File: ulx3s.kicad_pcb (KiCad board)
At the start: 4 copper layers, 94 x 50.8 mm, 222 parts, among them J1 CONN_02X20, J2 CONN_02X20, J3 WIFI_OFF, J4 CONN_02X03, J5 VJ1, Q1 BC857, Q2 2N7002, SW1 SW_DIP_x04, U1 LFE5U-85F-6BG381C, U10 IS25LP128F-JBLE, U11 PCA9306D, U2 MT48LC16M16A2TG, U3 TLV62569DBV, U4 TLV62569DBV, U5 TLV62569DBV, U6 FT231XS, U7 MCP7940NT, U8 MAX11125, U9 ESP32, Y1 FNETHE025, Y2 32768Hz

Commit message: First pass cleanup
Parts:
- removed AE1: 433MHz, TestPoint:TestPoint_Pad_D1.0mm
- removed AUDIO1: JACK_TRS_6PINS, audio-jack:CUI_SJ-43516-SMT
- removed B0, B1, B2, B3, B4, B5, B6: PTS645, Button_Switch_SMD:SW_SPST_PTS645
- removed BAT1: CR1225, Keystone_3000_1x12mm-CoinCell:Keystone_3000_1x12mm-CoinCell
- removed C14, C59, C60, C62: 220nF, Capacitor_SMD:C_0603_1608Metric
- removed C15, C21, C54, C55, C58, C61: 22uF, Capacitor_SMD:C_0805_2012Metric
- removed C16, C47: 2.2uF, Capacitor_SMD:C_0805_2012Metric
- removed C18: 470pF, Capacitor_SMD:C_0603_1608Metric
- removed C33, C34, C35, C52: 22nF, Capacitor_SMD:C_0603_1608Metric
- removed C56, C57: 4.7pF, Capacitor_SMD:C_0603_1608Metric
- removed D0, D11, D4: RED, LED_SMD:LED_0805_2012Metric
- removed D1, D5: ORANGE, LED_SMD:LED_0805_2012Metric
- removed D10, D13, D14, D16, D17, D27: 1N914, Diode_SMD:D_SOD-323_HandSoldering
- removed D12, D15: BAT54W, Diode_SMD:D_SOD-323_HandSoldering
- removed D2, D6: GREEN, LED_SMD:LED_0805_2012Metric
- removed D3, D7: BLUE, LED_SMD:LED_0805_2012Metric
- removed D51, D52: 0, jumper:D_SMA_Jumper_NC
- removed HR: HR, hrvatski_proizvod_veci:hrvatski
- removed J1, J2: CONN_02X20, Socket_Strips:Socket_Strip_Angled_2x20
- removed J3: WIFI_OFF, Connector_PinHeader_2.54mm:PinHeader_1x02_P2.54mm_Vertical
- removed J5: VJ1, Connector_PinHeader_2.54mm:PinHeader_1x03_P2.54mm_Vertical
- removed L4, L5: 33uH, Inductor_SMD:L_0805_2012Metric_Pad1.15x1.40mm_HandSolder
- removed LCD1: ST7789, st7789:st7789
- removed Q1: BC857, Package_TO_SOT_SMD:SOT-23
- removed Q2: 2N7002, Package_TO_SOT_SMD:SOT-23
- removed R1, R25, R26, R3, R4: 4.7k, Resistor_SMD:R_0603_1608Metric
- removed R10, R17, R21, R39, R51, R60, R7: 130, Resistor_SMD:R_0603_1608Metric
- removed R13, R34, R9: 15k, Resistor_SMD:R_0603_1608Metric
- removed R14, R18, R57, R6, R66, R8: 1.1k, Resistor_SMD:R_0603_1608Metric
- removed R15, R19, R35, R41, R42, R43, R44, R45, R46, R47, R48, R58, R65: 549, Resistor_SMD:R_0603_1608Metric
- removed R16, R20, R59: 270, Resistor_SMD:R_0603_1608Metric
- removed R2: 18k, Resistor_SMD:R_0603_1608Metric
- removed R22, R23: 3.3k, Resistor_SMD:R_0603_1608Metric
- removed R24: 100k, Resistor_SMD:R_0603_1608Metric
- removed R38: 0.47, Resistor_SMD:R_0603_1608Metric
- removed R5: 2.2M, Resistor_SMD:R_0603_1608Metric
- removed R56: 0, Resistor_SMD:R_0603_1608Metric
- removed REF** (x2): emard12mm, emard:emard12mm
- removed REF**: inem, inem:inem
- removed RV2, RV3: 0, Resistor_SMD:R_0805_2012Metric_Pad1.29x1.40mm_HandSolder
- removed SD1: 104031-0811, micro-sd-104031-811:MOLEX_104031-0811
- removed SW1: SW_DIP_x04, dipswitch:SW_DIP_x4_W8.61mm_Slide_LowProfile
- removed U11: PCA9306D, SM8:SM8
- removed U2: MT48LC16M16A2TG, TSOP54:TSOP54
- removed U6: FT231XS, ft231x:FT231X-SSOP-20_4.4x6.5mm_Pitch0.65mm
- removed U7: MCP7940NT, SOT96-1:SOT96-1
- removed U8: MAX11125, max1112x-tqfn28:MAX1112x-TQFN-28-1EP_5x5mm_Pitch0.5mm
- removed U9: ESP32, ESP32:ESP32
- removed Y2: 32768Hz, abs25:Crystal_SMD_ABS25
- removed fer: fer, fer:fer
- removed koncar: koncar, koncar:koncar
- removed radiona: radiona, radiona:radiona
- C13: moved to F.Cu
- moved C13 46.9 mm to (133.6, 59.5), turned to 0 degrees
- moved C51 17.8 mm to (162.7, 98.2)
- moved C50 11.6 mm to (169.2, 81.9)
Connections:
- C13 pad 1: +5V -> GND
- C13 pad 2: /power/WKUP -> 2V5_3V3
- C20 pad 1: +3V3 -> 2V5_3V3
- C25 pad 1: +3V3 -> 2V5_3V3
- C31 pad 1: +3V3 -> 2V5_3V3
- C32 pad 1: +3V3 -> 2V5_3V3
- C46 pad 1: +3V3 -> 2V5_3V3
- C50 pad 1: +3V3 -> 2V5_3V3
- C51 pad 1: +3V3 -> 2V5_3V3
- D18 pad 2: FTDI_nSLEEP -> (no net)
- D19 pad 2: FT2V5 -> (no net)
- D28 pad 1: PWRBTn -> (no net)
- GPDI1 pad 15: GPDI_SCL -> (no net)
- GPDI1 pad 16: GPDI_SDA -> (no net)
- J4 pad 2: +3V3 -> 2V5_3V3
- R11 pad 1: +3V3 -> 2V5_3V3
- R12 pad 1: +3V3 -> 2V5_3V3
- R27 pad 1: +3V3 -> 2V5_3V3
- R28 pad 1: +3V3 -> 2V5_3V3
- R29 pad 1: +3V3 -> 2V5_3V3
- R30 pad 1: +3V3 -> 2V5_3V3
- R31 pad 1: +3V3 -> 2V5_3V3
- R32 pad 1: +3V3 -> 2V5_3V3
- R33 pad 1: +3V3 -> 2V5_3V3
- R37 pad 1: FTDI_nTXLED -> (no net)
- R49 pad 1: USB_FTDI_D- -> (no net)
- R50 pad 1: USB_FTDI_D+ -> (no net)
- R62 pad 2: +3V3 -> 2V5_3V3
- RP3 pad 2: +3V3 -> 2V5_3V3
- U1 pad A10: GP1 -> (no net)
- U1 pad A11: GN1 -> (no net)
- U1 pad A15: Net-(U1-PadA15) -> (no net)
- U1 pad A2: GP9 -> (no net)
- U1 pad A3: AUDIO_R0 -> (no net)
- U1 pad A4: GP8 -> (no net)
- U1 pad A5: GN8 -> (no net)
- U1 pad A6: GP7 -> (no net)
- U1 pad A7: GP4 -> (no net)
- U1 pad A8: GN4 -> (no net)
- U1 pad A9: GP2 -> (no net)
- U1 pad B1: GN9 -> (no net)
- U1 pad B10: GN2 -> (no net)
- U1 pad B11: GP0 -> (no net)
- U1 pad B13: GP26 -> (no net)
- U1 pad B15: GP22 -> (no net)
- U1 pad B17: GP23 -> (no net)
- U1 pad B19: FPDI_SDA -> (no net)
- U1 pad B2: LED0 -> (no net)
- U1 pad B3: AUDIO_L3 -> (no net)
- U1 pad B4: GN10 -> (no net)
- U1 pad B5: AUDIO_R1 -> (no net)
- U1 pad B6: GN7 -> (no net)
- U1 pad B8: GN5 -> (no net)
- U1 pad B9: GP3 -> (no net)
- U1 pad C1: LED2 -> (no net)
- U1 pad C10: GN3 -> (no net)
- U1 pad C11: GN0 -> (no net)
- U1 pad C13: GN26 -> (no net)
- U1 pad C15: GN22 -> (no net)
- U1 pad C16: GP24 -> (no net)
- U1 pad C17: GN23 -> (no net)
- U1 pad C18: GP21 -> (no net)
- U1 pad C2: LED1 -> (no net)
- U1 pad C20: SDRAM_D11 -> (no net)
- U1 pad C3: AUDIO_L2 -> (no net)
- U1 pad C4: GP10 -> (no net)
- U1 pad C5: AUDIO_R3 -> (no net)
- U1 pad C6: GP6 -> (no net)
- U1 pad C7: GN6 -> (no net)
- U1 pad C8: GP5 -> (no net)
- U1 pad C9: Net-(U1-PadC9) -> (no net)
- U1 pad D1: LED4 -> (no net)
- U1 pad D10: Net-(U1-PadD10) -> (no net)
- U1 pad D11: Net-(U1-PadD11) -> (no net)
- U1 pad D12: Net-(U1-PadD12) -> (no net)
- U1 pad D13: GP27 -> (no net)
- U1 pad D14: GP25 -> (no net)
- U1 pad D16: GN24 -> (no net)
- U1 pad D17: GN21 -> (no net)
- U1 pad D18: GP20 -> (no net)
- U1 pad D19: SDRAM_D10 -> (no net)
- U1 pad D2: LED3 -> (no net)
- U1 pad D20: SDRAM_D9 -> (no net)
- U1 pad D3: AUDIO_L1 -> (no net)
- U1 pad D5: AUDIO_R2 -> (no net)
- U1 pad D6: BTN_PWRn -> (no net)
- U1 pad D7: SW3 -> (no net)
- U1 pad D8: SW2 -> (no net)
- U1 pad D9: Net-(U1-PadD9) -> (no net)
- U1 pad E1: LED6 -> (no net)
- U1 pad E10: Net-(U1-PadE10) -> (no net)
- U1 pad E11: Net-(U1-PadE11) -> (no net)
- U1 pad E12: FPDI_SCL -> (no net)
- U1 pad E13: GN27 -> (no net)
- U1 pad E14: GN25 -> (no net)
- U1 pad E17: GN20 -> (no net)
- U1 pad E18: SDRAM_D12 -> (no net)
- U1 pad E19: SDRAM_D8 -> (no net)
- U1 pad E2: LED5 -> (no net)
- U1 pad E20: SDRAM_DQM1 -> (no net)
- U1 pad E3: GN11 -> (no net)
- U1 pad E4: AUDIO_L0 -> (no net)
- U1 pad E5: AUDIO_V3 -> (no net)
- U1 pad E6: WIFI_GPIO35 -> (no net)
- U1 pad E7: SW4 -> (no net)
- U1 pad E8: SW1 -> (no net)
- U1 pad E9: WIFI_GPIO25 -> (no net)
- U1 pad F1: WIFI_EN -> (no net)
- U1 pad F11: +3V3 -> 2V5_3V3
- U1 pad F12: +3V3 -> 2V5_3V3
- U1 pad F17: GP19 -> (no net)
- U1 pad F18: SDRAM_D13 -> (no net)
- U1 pad F19: SDRAM_CLK -> (no net)
- U1 pad F2: AUDIO_V1 -> (no net)
- U1 pad F20: SDRAM_CKE -> (no net)
- U1 pad F3: GN12 -> (no net)
- U1 pad F4: GP11 -> (no net)
- U1 pad F5: AUDIO_V2 -> (no net)
- U1 pad G16: SHUTDOWN -> (no net)
- U1 pad G18: GN19 -> (no net)
- U1 pad G19: SDRAM_A12 -> (no net)
- U1 pad G20: SDRAM_A11 -> (no net)
- U1 pad G3: GP12 -> (no net)
- U1 pad G5: GN13 -> (no net)
- U1 pad H1: SD_D1 -> (no net)
- U1 pad H14: +3V3 -> 2V5_3V3
- U1 pad H15: +3V3 -> 2V5_3V3
- U1 pad H16: BTN_R -> (no net)
- U1 pad H17: GN18 -> (no net)
- U1 pad H18: GP18 -> (no net)
- U1 pad H2: SD_CLK -> (no net)
- U1 pad H20: SDRAM_A9 -> (no net)
- U1 pad H3: LED7 -> (no net)
- U1 pad H4: GP13 -> (no net)
- U1 pad H5: AUDIO_V0 -> (no net)
- U1 pad J1: SD_CMD -> (no net)
- U1 pad J15: +3V3 -> 2V5_3V3
- U1 pad J16: SDRAM_D0 -> (no net)
- U1 pad J17: SDRAM_D15 -> (no net)
- U1 pad J18: SDRAM_D14 -> (no net)
- U1 pad J19: SDRAM_A8 -> (no net)
- U1 pad J20: SDRAM_A7 -> (no net)
- U1 pad J3: SD_D0 -> (no net)
- U1 pad J4: OLED_BL -> (no net)
- U1 pad J5: WIFI_GPIO22 -> (no net)
- U1 pad K1: SD_D2 -> (no net)
- U1 pad K16: Net-(U1-PadK16) -> (no net)
- U1 pad K17: Net-(U1-PadK17) -> (no net)
- U1 pad K18: SDRAM_A6 -> (no net)
- U1 pad K19: SDRAM_A5 -> (no net)
- U1 pad K2: SD_D3 -> (no net)
- U1 pad K20: SDRAM_A4 -> (no net)
- U1 pad K3: WIFI_RXD -> (no net)
- U1 pad K4: WIFI_TXD -> (no net)
- U1 pad K5: WIFI_GPIO21 -> (no net)
- U1 pad L1: WIFI_GPIO26 -> (no net)
- U1 pad L14: +3V3 -> 2V5_3V3
- U1 pad L15: +3V3 -> 2V5_3V3
- U1 pad L16: GP17 -> (no net)
- U1 pad L17: GN17 -> (no net)
- U1 pad L18: SDRAM_D1 -> (no net)
- U1 pad L19: SDRAM_A3 -> (no net)
- U1 pad L2: WIFI_GPIO0 -> (no net)
- U1 pad L20: SDRAM_A2 -> (no net)
- U1 pad L3: FTDI_TXDEN -> (no net)
- U1 pad L4: FTDI_RXD -> (no net)
- U1 pad L5: FTDI_nRXLED -> (no net)
- U1 pad L6: +3V3 -> 2V5_3V3
- U1 pad L7: +3V3 -> 2V5_3V3
- U1 pad M1: FTDI_TXD -> (no net)
- U1 pad M15: +3V3 -> 2V5_3V3
- U1 pad M17: GN16 -> (no net)
- U1 pad M18: SDRAM_D2 -> (no net)
- U1 pad M19: SDRAM_A1 -> (no net)
- U1 pad M20: SDRAM_A0 -> (no net)
- U1 pad M3: FTDI_nRTS -> (no net)
- U1 pad M5: Net-(U1-PadM5) -> (no net)
- U1 pad M6: +3V3 -> 2V5_3V3
- U1 pad N1: FTDI_nDTR -> (no net)
- U1 pad N16: GP16 -> (no net)
- U1 pad N17: GP15 -> (no net)
- U1 pad N18: SDRAM_D3 -> (no net)
- U1 pad N19: SDRAM_A10 -> (no net)
- U1 pad N2: OLED_CS -> (no net)
- U1 pad N20: SDRAM_BA1 -> (no net)
- U1 pad N3: WIFI_GPIO27 -> (no net)
- U1 pad N4: WIFI_GPIO19 -> (no net)
- U1 pad N5: SD_CD -> (no net)
- U1 pad P1: OLED_DC -> (no net)
- U1 pad P10: +3V3 -> 2V5_3V3
- U1 pad P16: GN15 -> (no net)
- U1 pad P17: ADC_SCLK -> (no net)
- U1 pad P18: SDRAM_D4 -> (no net)
- U1 pad P19: SDRAM_BA0 -> (no net)
- U1 pad P2: OLED_RES -> (no net)
- U1 pad P20: SDRAM_nCS -> (no net)
- U1 pad P3: OLED_MOSI -> (no net)
- U1 pad P4: OLED_CLK -> (no net)
- U1 pad P5: SD_WP -> (no net)
- U1 pad P9: +3V3 -> 2V5_3V3
- U1 pad R1: BTN_F1 -> (no net)
- U1 pad R16: ADC_MOSI -> (no net)
- U1 pad R17: ADC_CSn -> (no net)
- U1 pad R18: BTN_U -> (no net)
- U1 pad R20: SDRAM_nRAS -> (no net)
- U1 pad R3: Net-(U1-PadR3) -> (no net)
- U1 pad T1: BTN_F2 -> (no net)
- U1 pad T16: Net-(U1-PadT16) -> (no net)
- U1 pad T17: SDRAM_D6 -> (no net)
- U1 pad T18: SDRAM_D5 -> (no net)
- U1 pad T19: SDRAM_nCAS -> (no net)
- U1 pad T2: +3V3 -> 2V5_3V3
- U1 pad T20: SDRAM_nWE -> (no net)
- U1 pad T3: +3V3 -> 2V5_3V3
- U1 pad T4: +3V3 -> 2V5_3V3
- U1 pad U1: BTN_L -> (no net)
- U1 pad U16: ADC_MISO -> (no net)
- U1 pad U17: GN14 -> (no net)
- U1 pad U18: GP14 -> (no net)
- U1 pad U19: SDRAM_DQM0 -> (no net)
- U1 pad U2: +3V3 -> 2V5_3V3
- U1 pad U20: SDRAM_D7 -> (no net)
- U1 pad V1: BTN_D -> (no net)
- U1 pad W13: Net-(U1-PadW13) -> (no net)
- U1 pad W14: Net-(U1-PadW14) -> (no net)
- U1 pad W17: Net-(U1-PadW17) -> (no net)
- U1 pad W18: Net-(U1-PadW18) -> (no net)
- U1 pad W20: Net-(U1-PadW20) -> (no net)
- U1 pad W4: Net-(U1-PadW4) -> (no net)
- U1 pad W5: Net-(U1-PadW5) -> (no net)
- U1 pad W8: Net-(U1-PadW8) -> (no net)
- U1 pad W9: Net-(U1-PadW9) -> (no net)
- U1 pad Y11: Net-(U1-PadY11) -> (no net)
- U1 pad Y12: Net-(U1-PadY12) -> (no net)
- U1 pad Y14: Net-(U1-PadY14) -> (no net)
- U1 pad Y15: Net-(U1-PadY15) -> (no net)
- U1 pad Y16: Net-(U1-PadY16) -> (no net)
- U1 pad Y17: Net-(U1-PadY17) -> (no net)
- U1 pad Y19: Net-(U1-PadY19) -> (no net)
- U1 pad Y5: Net-(U1-PadY5) -> (no net)
- U1 pad Y6: Net-(U1-PadY6) -> (no net)
- U1 pad Y7: Net-(U1-PadY7) -> (no net)
- U1 pad Y8: Net-(U1-PadY8) -> (no net)
- U10 pad 8: +3V3 -> 2V5_3V3
- U3 pad 1: /power/PWREN -> +5V
- U4 pad 1: /power/PWREN -> +5V
- U5 pad 1: /power/PWREN -> +5V
- US1 pad 4: Net-(US1-Pad4) -> (no net)
- US2 pad 4: US2_ID -> (no net)
- Y1 pad 1: +3V3 -> 2V5_3V3
- Y1 pad 4: +3V3 -> 2V5_3V3
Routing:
- net (no net): track 0.00 -> 834.9 mm, vias 0 -> 160
- net +3V3: track 184.1 -> 0.00 mm, vias 33 -> 0
- net GND: track 458.6 -> 304.4 mm, vias 136 -> 124
- net /power/PWREN: track 115.6 -> 0.00 mm, vias 3 -> 0
- net /usb/ANT_433MHz: track 111.7 -> 4.23 mm, vias 2 -> 0
- net FPDI_SDA: track 91.9 -> 0.00 mm, vias 6 -> 0
- net FPDI_SCL: track 89.0 -> 0.00 mm, vias 4 -> 0
- net +5V: track 149.0 -> 233.3 mm, vias 7 -> 9
- net /blinkey/BTNPUR: track 76.6 -> 0.00 mm, vias 3 -> 0
- net BTN_R: track 70.5 -> 0.00 mm, vias 4 -> 0
- net GP15: track 58.6 -> 0.00 mm, vias 2 -> 0
- net USB_FTDI_D+: track 58.5 -> 0.00 mm, vias 2 -> 0
- net GP14: track 58.1 -> 0.00 mm, vias 1 -> 0
- net GP17: track 58.0 -> 0.00 mm, vias 2 -> 0
- net GP16: track 57.0 -> 0.00 mm, vias 1 -> 0
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- removed copper zone on In1.Cu, net +3V3
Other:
- board text removed: "+-"
- board text removed: "-+"
- board text removed: "0"
- board text removed: "1"
- board text removed: "10"
- board text removed: "11"
- board text removed: "12"
- board text removed: "13"
- board text removed: "14"
- board text removed: "15"
- board text removed: "16"
- board text removed: "17"
- board text removed: "18"
- board text removed: "19"
- board text removed: "2"
- board text removed: "2.5/3.3V"
- board text removed: "2.5V"
- board text removed: "20"
- board text removed: "21"
- board text removed: "22"
- board text removed: "23"
- board text removed: "24"
- board text removed: "25"
- board text removed: "26"
- board text removed: "27"
- board text removed: "3"
- board text removed: "3.3V"
- board text removed: "3V 12.5x2.5mm"
- board text removed: "4"
- board text removed: "5"
- board text removed: "5V"
- board text removed: "6"
- board text removed: "7"
- board text removed: "8"
- board text removed: "9"
- board text removed: "ADC"
- board text removed: "CR1225"
- board text removed: "DOWN"
- board text removed: "F1"
- board text removed: "F2"
- board text removed: "LEFT"
- board text removed: "PWR"
- board text removed: "RIGHT"
- board text removed: "RTC"
- board text removed: "SDRAM"
- board text removed: "UP"
- board text removed: "skriptarnica.hr"

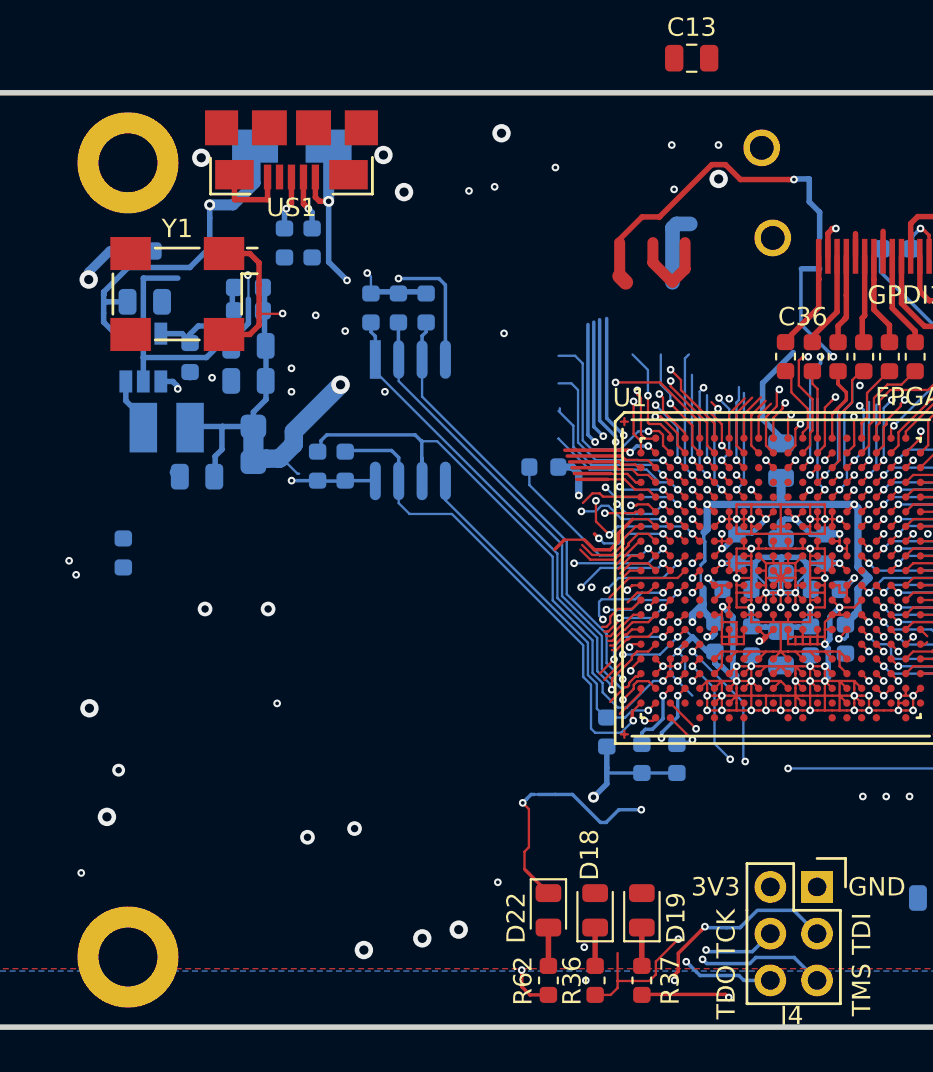
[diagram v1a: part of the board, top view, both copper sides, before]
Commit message: More cleanup - moving flash and crystal
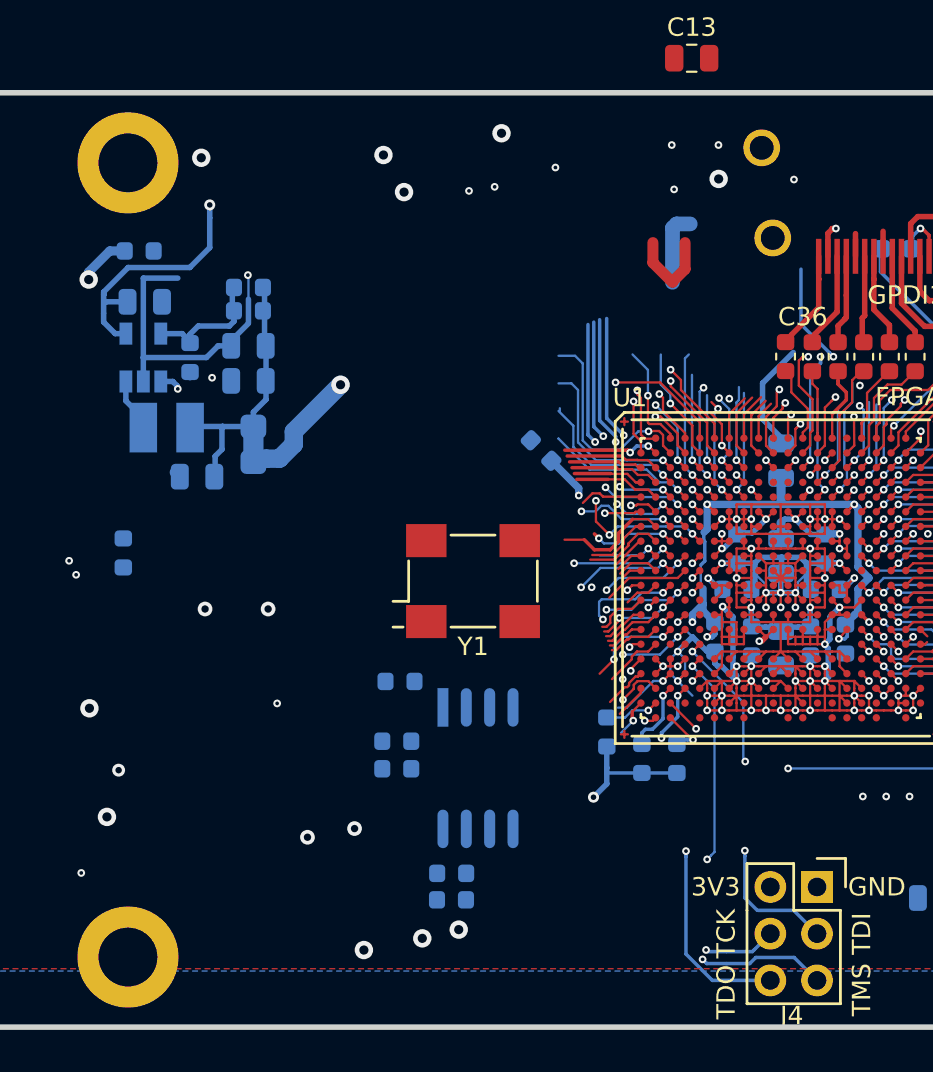
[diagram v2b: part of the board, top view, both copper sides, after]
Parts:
- removed D18: GREEN, LED_SMD:LED_0805_2012Metric
- removed D19: RED, LED_SMD:LED_0805_2012Metric
- removed D22: BLUE, LED_SMD:LED_0805_2012Metric
- removed D8: STPS2L40AF, Diode_SMD:D_SMA
- removed R36, R37, R62: 549, Resistor_SMD:R_0603_1608Metric
- removed R49, R50: 27, Resistor_SMD:R_0603_1608Metric
- removed US1: MICRO_USB, usb_otg:USB-MICRO-B-FCI-10118192-0001LF
- moved R11 25.1 mm to (117.6, 98.2), turned to 0 degrees
- moved R29 24.7 mm to (120.6, 105.3), turned to 0 degrees
- moved R28 23.6 mm to (117.6, 96.7), turned to 0 degrees
- moved R12 22.9 mm to (120.6, 103.9), turned to 0 degrees
- moved Y1 22.4 mm to (121.8, 88.0), turned to 0 degrees
- moved R30 20.4 mm to (117.8, 93.4), turned to 0 degrees
- moved U10 19.3 mm to (122.0, 98.1)
- moved C53 0.91 mm to (125.5, 80.9), turned to 135 degrees
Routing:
- net USB5V: track 52.1 -> 0.00 mm, vias 3 -> 0
- net /flash/FLASH_SCK: track 32.7 -> 3.62 mm
- net /flash/FLASH_nCS: track 29.6 -> 3.25 mm, vias 1 -> 0
- net GND: track 304.4 -> 278.2 mm, vias 124 -> 117
- net /flash/FLASH_MISO: track 28.3 -> 2.49 mm
- net /flash/FLASH_nHOLD: track 27.3 -> 2.11 mm
- net /flash/FLASH_nWP: track 27.4 -> 3.43 mm
- net +2V5: track 123.8 -> 103.7 mm
- net 2V5_3V3: track 174.1 -> 154.0 mm, vias 30 -> 25
- net /flash/FLASH_MOSI: track 19.5 -> 2.98 mm
- net JTAG_TMS: track 39.4 -> 23.2 mm, vias 4 -> 2
- net (no net): track 834.9 -> 820.1 mm, vias 160 -> 159
- net JTAG_TDO: track 35.1 -> 20.7 mm, vias 4 -> 3
- net JTAG_TDI: track 33.7 -> 19.9 mm, vias 5 -> 3
- net +5V: track 233.3 -> 228.4 mm
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
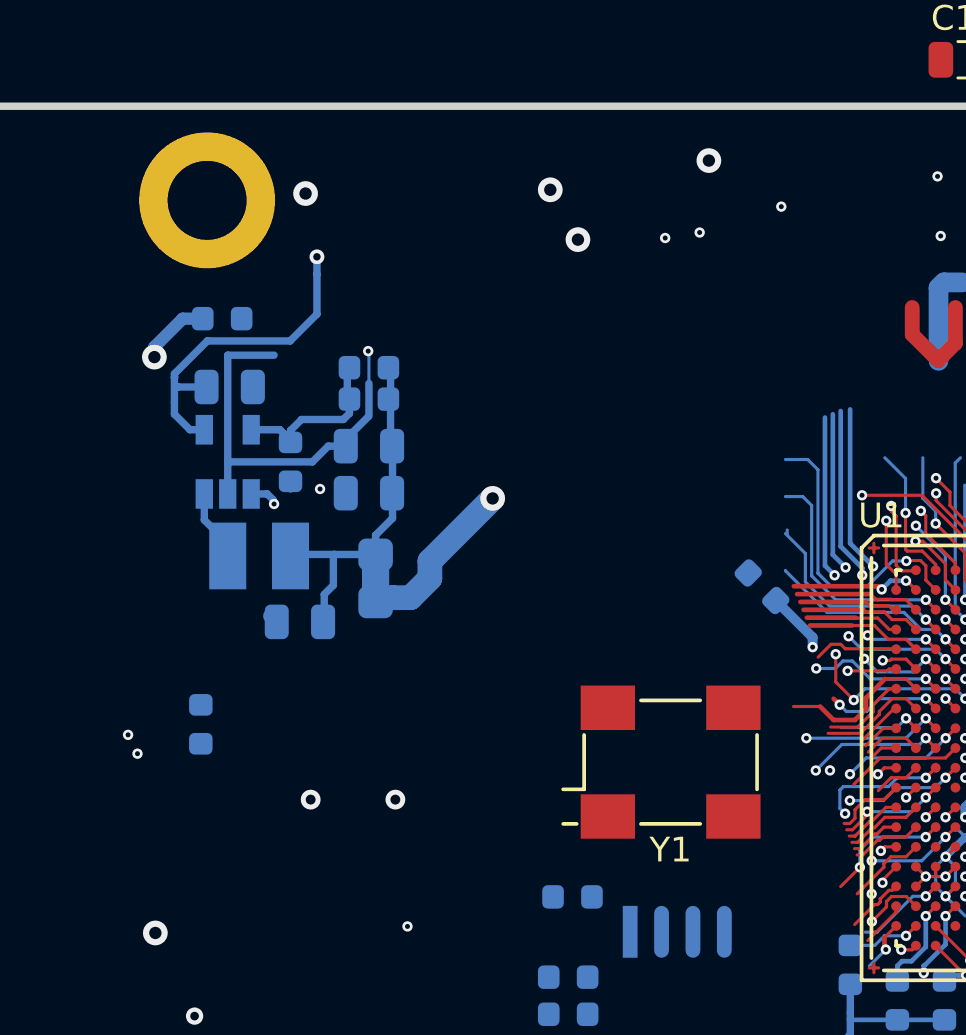
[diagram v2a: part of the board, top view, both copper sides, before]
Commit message: Moving power closer
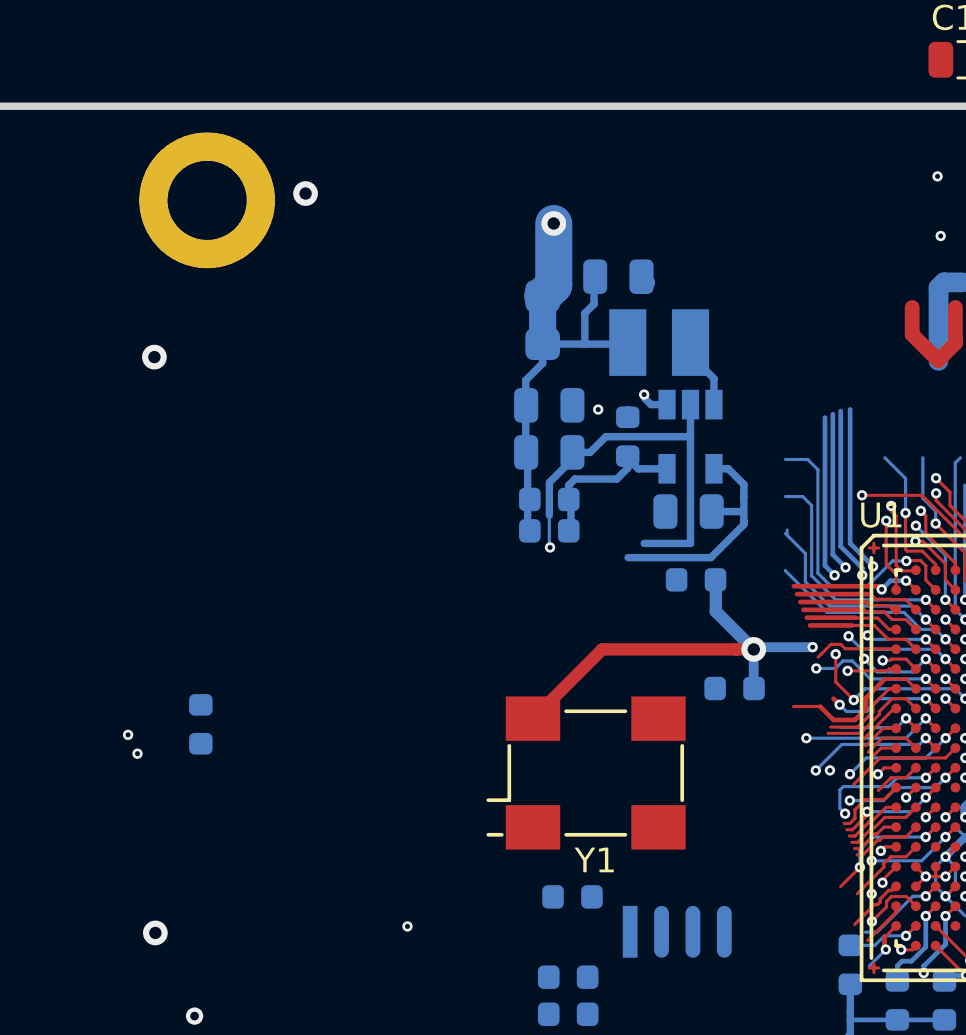
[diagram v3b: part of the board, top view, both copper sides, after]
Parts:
- moved C48 21.9 mm to (122.8, 80.6), turned to 180 degrees
- moved C1 19.2 mm to (122.5, 77.8), turned to 180 degrees
- moved C23 19.0 mm to (119.6, 68.3), turned to 0 degrees
- moved U4 18.8 mm to (122.6, 74.8), turned to 0 degrees
- moved L2 18.4 mm to (121.3, 71.0), turned to 180 degrees
- moved RB2 13.7 mm to (120.0, 74.8), turned to 270 degrees
- moved RP2 12.4 mm to (116.6, 70.1), turned to 90 degrees
- moved C10 9.84 mm to (116.8, 78.6), turned to 0 degrees
- moved RA2 8.36 mm to (116.8, 77.3), turned to 0 degrees
- moved C12 8.12 mm to (116.8, 73.5), turned to 0 degrees
- moved C11 7.31 mm to (116.8, 75.4), turned to 0 degrees
- moved C53 4.27 mm to (124.3, 85.0), turned to 180 degrees
- moved Y1 3.06 mm to (118.7, 88.4)
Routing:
- net +5V: track 228.4 -> 158.3 mm, vias 9 -> 7
- net 2V5_3V3: track 154.0 -> 138.6 mm, vias 25 -> 26
- net +2V5: track 103.7 -> 98.0 mm
- net GND: vias 117 -> 110
